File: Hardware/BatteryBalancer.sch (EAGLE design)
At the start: 49 parts, among them J2 ICSP, U3 SINGLECELL, U4 ATMEGA328P_TQFP, U5 SINGLECELL, U6 SINGLECELL, U7 SINGLECELL, Y1 16MHz

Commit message: Going home
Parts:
- removed JP10: JP10, SparkFun-Connectors:M08SMD-COMBO
- removed JP11: IOL, SparkFun-Connectors:M08SMD-COMBO
- removed JP13: AD, SparkFun-Connectors:M06SMD-STRAIGHT-COMBO
- added C11, C12, C13, C14, C18: 0.1uF, SparkFun-Capacitors:0.1UF-0603-25V-(+80/-20%)
- added C15: 10uF, SparkFun-Capacitors:10UF-POLAR-EIA3216-16V-10%(TANT)
- added C17: 10nF, SparkFun-Capacitors:10NF-0603-50V-10%
- added D2: GREEN, SparkFun-LED:LED-GREENLILYPAD
- added D3: YELLOW, SparkFun-LED:LED-YELLOW_HIDDENSILK
- added F1: 6V 0.5A, SparkFun-Fuses:PPTC_6V500MA
- added J1: (no value), SparkFun-Connectors:USB_MICRO-B_HALF_PTH_MILL
- added LED1: Blue, SparkFun-LED:LED-BLUE_HIDDENSILK
- added R1, R24: 10k, SparkFun-Resistors:10KOHM-0603-1/10W-1%
- added R25, R26: 4.7k, SparkFun-Resistors:4.7KOHM-0603-1/10W-1%
- added U1: CH340C, SparkFun-IC-Comms:CH340C
- added U10, U11, U2, U8, U9: TAP_POINT, BBLib:TAP_POINT
- J2: value ICSP -> ISP
- R3: value 10k -> 4.7k; device SparkFun-Resistors:10KOHM-0603-1/10W-1% -> SparkFun-Resistors:4.7KOHM-0603-1/10W-1%
- S1: value RESET -> Tall Switch; device SparkFun-Electromechanical:SWITCH_SPST_4_PINSQUARE -> SparkFun-Switches:MOMENTARY-SWITCH-SPST-SMD-5.2-TALL-REDUNDANT
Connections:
- removed net 3.3V: JP10.5
- removed net 5V: C2.2, J2.2, JP10.4, JP10.7, R3.2, U4.AVCC, U4.VCC@4, U4.VCC@6
- removed net AD0: JP13.1, U4.PC0(ADC0)
- removed net AD1: JP13.2, U4.PC1(ADC1)
- removed net AD2: JP13.3, U4.PC2(ADC2)
- removed net AD3: JP13.4, U4.PC3(ADC3)
- removed net AD4/SDA: JP13.5, U4.PC4(ADC4/SDA)
- removed net AD5/SCL: JP13.6, U4.PC5(ADC5/SCL)
- removed net IO2: JP11.3, U4.PD2(INT0)
- removed net IO3: JP11.4, U4.PD3(INT1)
- removed net IO4: JP11.5, U4.PD4(XCK/T0)
- removed net IO5: JP11.6, U4.PD5(T1)
- removed net IO6: JP11.7, U4.PD6(AIN0)
- removed net IO7: JP11.8, U4.PD7(AIN1)
- removed net IO8: U4.PB0(ICP)
- removed net IO9: U4.PB1(OC1A)
- removed net VIN: JP10.1
- new net !DTR: C12.1, U1.!DTR
- new net !PD: R1.1, U$2.!PD
- new net AREF: C2.1, U4.AREF
- new net D+: J1.D+, U1.UD+
- new net D-: J1.D-, U1.UD-
- new net N$1: LED1.A, R3.2
- new net N$36: D3.A, R25.1
- new net SHLD: J1.SHIELD
- new net USBVCC: C14.1, C15.+, F1.2
- new net VBATT: R16.2, R2.2, R7.1, U$2.VDD, U11.1, U5.+
- new net VCC: C11.2, C18.1, J2.2, R24.2, R25.2, R26.2, U1.VCC, U4.AVCC, U4.VCC
- new net VUSB: C13.1, F1.1, J1.VBUS
- net GND: now also C11.1, C13.2, C14.2, C15.-, C17.2, C18.2, C2.2, J1.GND, LED1.C, U1.GND, U2.1, U4.GND; no longer C2.1, JP10.2, JP10.3, S1.2, U4.GND@3, U4.GND@5
- net N$10: now also U8.1
- net N$2: now also D2.A, R26.1; no longer R16.2, R2.2, R7.1, U$2.VDD, U5.+
- net N$23: now also R1.2
- net N$38: now also C17.1, U1.V3; no longer U$2.!PD
- net N$6: now also U10.1
- net N$8: now also U9.1
- net RESET: now also C12.2, R24.1, S1.2; no longer JP10.6, R3.1, S1.3, S1.4
- net RX-I: now also D3.C, U1.TXO; no longer JP11.1
- net SCLK: now also R3.1
- net TX-O: now also D2.C, U1.RXI; no longer JP11.2
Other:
- note added: "USB-to-Serial Converter"
- moved on the sheet: C2, J2, R3, Y1

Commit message: going home
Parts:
- added C16: 10uF, SparkFun-Capacitors:10UF-POLAR-EIA3216-16V-10%(TANT)
- added C19: 0.1uF, SparkFun-Capacitors:0.1UF-0603-25V-(+80/-20%)
- added C20: 47uF, SparkFun-Capacitors:47UF-POLAR-PANASONIC_D-35V-20%
- added D1: TH, SparkFun-DiscreteSemi:DIODE-ZENER-MMBZ5233BLT1G
- added D4: MATCH, SparkFun-DiscreteSemi:DIODE-ZENER-MMBZ5233BLT1G
- added IC1: OP-AMP, SparkFun-IC-Amplifiers:OPAMP-DUALU
- added IC3: LM1117, Testing:V_REG_LM1117ALT1
- added Q4: (no value), MTAES_V2_UniqueParts:AMP_MOSFET_NCH-2N7002K
- added Q5: 4.3A/20V/54mΩ, SparkFun-DiscreteSemi:MOSFET_PCH-IRLML2244
- added R27: 1M, SparkFun-Resistors:1MOHM-0603-1/4W-5%
- added R28: 330k, SparkFun-Resistors:330KOHM-0603-1/10W-1%
- added R29: 715, SparkFun-Resistors:715OHM-0603-1/10W-1%
- added R30: 240, SparkFun-Resistors:240OHM-0603-1/10W-1%
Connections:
- removed net VBATT: R16.2, R2.2, R7.1, U$2.VDD, U11.1, U5.+
- new net 5V: C16.+, C19.1, IC3.OUT, IC3.OUT@1, R30.2
- new net CHARGE: IC1G1.OUT
- new net N$39: IC3.ADJ, R29.2, R30.1
- new net N$40: D4.C, IC1G1.+IN, R27.1
- new net N$41: D1.C, IC1G1.-IN, R28.1
- new net V_BATT: C20.+, IC1G3.P$V+, IC3.IN, Q5.S, R27.2, R28.2
- new net V_RAW: Q5.D, R16.2, R2.2, R7.1, U$2.VDD, U11.1, U5.+
- net GND: now also C16.-, C19.2, C20.-, D1.A, D4.A, IC1G3.P$V-, Q5.G, R29.1
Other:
- note added: "P-channel MOSFET for reverse polarity protection"
- note added: "Power Supply"
- note added: "This comparator will be HIGH when the voltage is greater than the Zener voltage of the THreshold diode, and LOW otherwise. The MATCH diode is used primarily to match the leakage current of the THreshold diode. Below V THreshold the leakage currents cause substantial voltage drop over the large-value current limiting resistors, sized so that the inverting input sees a higher voltage. When the batt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"
- moved on the sheet: R17, R18, R19, R20, R21, R22, R23

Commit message: Schematic mostly done, starting layout
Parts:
- removed IC3: LM1117, Testing:V_REG_LM1117ALT1
- removed Q4: (no value), MTAES_V2_UniqueParts:AMP_MOSFET_NCH-2N7002K
- removed R20, R21, R22: 10k, SparkFun-Resistors:10KOHM-0603-1/10W-1%
- added C21: 1.0uF, SparkFun-Capacitors:1.0UF-1206-50V-10%
- added D10, D11, D7, D8, D9: BLUE, SparkFun-LED:LED-BLUE0603
- added D5, D6: 3A/10V/280mV, SparkFun-DiscreteSemi:DIODE-SCHOTTKY-BAT60A
- added JP1: VCC, SparkFun-Jumpers:JUMPER-SMT_2_NC_TRACE_SILK
- added Q6: (no value), MTAES_V2_UniqueParts:AMP_MOSFET_NCH-2N7002K
- added R31, R32: 1k, SparkFun-Resistors:1KOHM-0603-1/10W-1%
- added R33, R34, R35: 10k, SparkFun-Resistors:10KOHM-0603-1/10W-1%
- added R40, R41, R42, R43: DNP, SparkFun-Resistors:1KOHM-HORIZ-1/4W-5%
- added S2: Force Charge, SparkFun-Switches:MOMENTARY-SWITCH-SPST-SMD-5.2-TALL-REDUNDANT
- added S3: TEST, SparkFun-Switches:MOMENTARY-SWITCH-SPST-SMD-5.2-TALL-REDUNDANT
- added U$1: MCP1755, BBLib:MCP1755
- C15, C16: value 10uF -> 1.0uF; device SparkFun-Capacitors:10UF-POLAR-EIA3216-16V-10%(TANT) -> SparkFun-Capacitors:1.0UF-0603-16V-10%-X7R
- C19: device SparkFun-Capacitors:0.1UF-0603-25V-(+80/-20%) -> SparkFun-Capacitors:0.1UF-0603-25V-5%
- C20: value 47uF -> 10uF; device SparkFun-Capacitors:47UF-POLAR-PANASONIC_D-35V-20% -> SparkFun-Capacitors:10UF-1210-50V-20%
- Q5: value 4.3A/20V/54mΩ -> MOSFET_PCH-IRLML2244
- R1, R24: value 10k -> 1k; device SparkFun-Resistors:10KOHM-0603-1/10W-1% -> SparkFun-Resistors:1KOHM-0603-1/10W-1%
- R29: value 715 -> 10k; device SparkFun-Resistors:715OHM-0603-1/10W-1% -> SparkFun-Resistors:10KOHM-0603-1/10W-1%
- R30: value 240 -> 10k; device SparkFun-Resistors:240OHM-0603-1/10W-1% -> SparkFun-Resistors:10KOHM-0603-1/10W-1%
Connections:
- removed net !PD: R1.1, U$2.!PD
- removed net N$35: R22.2, U$2.AUX1
- removed net SCK: J2.3
- new net !CVNST: R34.1, U$2.!CNVST, U4.ADC7
- new net LED1: D7.A, U4.PC0(ADC0)
- new net LED2: D8.A, U4.PC1(ADC1)
- new net LED3: D9.A, U4.PC2(ADC2)
- new net LED4: D10.A, U4.PC3(ADC3)
- new net N$42: D9.C, R31.2
- new net N$43: D8.C, R24.2
- new net N$44: D7.C, R1.2
- new net TEST: D11.A, S3.1, U4.ADC6
- net !CS: now also R35.1
- net 5V: now also C16.1, D5.A, JP1.1, U$1.OUT; no longer C16.+, IC3.OUT, IC3.OUT@1, R30.2
- net ALERT: now also R33.1, U4.PD2(INT0)
- net CHARGE: now also Q6.D
- net GND: now also C15.2, C16.2, C20.2, C21.2, R1.1, R19.1, R23.1, R24.1, R31.1, R32.1, U$1.GND; no longer C15.-, C16.-, C20.-, R29.1
- net N$23: now also R43.2, U$2.AUX1; no longer C6.1, C7.1, C8.1, R1.2, U$2.AVCC, U$2.DVCC, U$2.VDRIVE, U$2.VREG
- net N$32: now also R42.2, U$2.AUX2; no longer R19.2, U$2.AUX4
- net N$33: now also R41.2; no longer R20.2
- net N$34: now also R40.2, U$2.AUX4; no longer R21.2, U$2.AUX2
- net N$37: now also D11.C, R19.2; no longer U$2.!CNVST
- net N$39: now also D10.C, R32.2; no longer IC3.ADJ, R29.2, R30.1
- net N$40: now also S2.1
- net RESET: now also Q6.S, R29.1, U$1.!SHDWN, U$2.!PD; no longer R24.1
- net SCLK: now also J2.3
- net USBVCC: now also C15.1, D6.A; no longer C15.+
- net VCC: now also D5.C, D6.C, JP1.2, Q6.G, R29.2, R33.2, R34.2, R35.2, S3.2; no longer R24.2
- net VREG: now also C6.1, C7.1, C8.1, R40.1, R41.1, R42.1, R43.1, U$2.AVCC, U$2.DVCC, U$2.VDRIVE, U$2.VREG; no longer R19.1, R20.1, R21.1, R22.1, R23.1
- net V_BATT: now also R30.2, S2.2, U$1.IN; no longer C20.+, IC3.IN
- net V_RAW: now also C20.1, C21.1
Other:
- note added: "Cut jumper is using USB-Serial"
- note added: "Maybe in the future this could incorporate a Schmitt Trigger to prevent switching too often"
- note added: "Probably don't need a pull on the op-amp line"
- note added: "This level shifter controls the reset line with the charge signal. When not charging Reset goes low. Reset has a pullup to VCC"
- note removed: "Power Supply"
- moved on the sheet: C1, C10, C19, C3, C4, C5, C6, C7, C8, C9, IC1G1, IC1G2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

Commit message: Routed 90%
Needs finishing routing and also pretty graphics
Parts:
- removed C15: 1.0uF, SparkFun-Capacitors:1.0UF-0603-16V-10%-X7R
- removed D10, D11: BLUE, SparkFun-LED:LED-BLUE0603
- removed F1: 6V 0.5A, SparkFun-Fuses:PPTC_6V500MA
- removed LED1: Blue, SparkFun-LED:LED-BLUE_HIDDENSILK
- removed Q10: (no value), MTAES_V2_UniqueParts:AMP_MOSFET_NCH-2N7002K
- removed R34, R35: 10k, SparkFun-Resistors:10KOHM-0603-1/10W-1%
- removed R40, R41, R42, R43: DNP, SparkFun-Resistors:1KOHM-HORIZ-1/4W-5%
- removed U$1: MCP1755, BBLib:MCP1755
- removed U$2: AD7280A, BBLib:AD7280A
- added JP2: RPP_BYP, SparkFun-Jumpers:JUMPER-SMT_2_NC_TRACE_SILK
- added Q4: (no value), MTAES_V2_UniqueParts:AMP_MOSFET_NCH-2N7002K
- added R20, R21, R22: DNP, BBLib:NTC_STOP_ONE_SIDE
- added U12: ATMEGA328P_TQFP, SparkFun-IC-Microcontroller:ATMEGA328P_TQFP
- added U13: CH340C, SparkFun-IC-Comms:CH340C
- C1: value 0.1uF -> 10uF; device SparkFun-Capacitors:0.1UF-0603-25V-5% -> SparkFun-Capacitors:10UF-1210-50V-20%
- C10, C6: value 1.0uF -> 0.1uF; device SparkFun-Capacitors:1.0UF-0603-16V-10%-X7R -> SparkFun-Capacitors:0.1UF-0603-25V-5%
- C11, C13: value 0.1uF -> 1.0uF; device SparkFun-Capacitors:0.1UF-0603-25V-(+80/-20%) -> SparkFun-Capacitors:1.0UF-0603-16V-10%-X7R
- C12: device SparkFun-Capacitors:0.1UF-0603-25V-(+80/-20%) -> SparkFun-Capacitors:0.1UF-0603-25V-5%
- C16: value 1.0uF -> 0.1uF; device SparkFun-Capacitors:1.0UF-0603-16V-10%-X7R -> SparkFun-Capacitors:0.1UF-0603-25V-(+80/-20%)
- C17: value 10nF -> 0.1uF; device SparkFun-Capacitors:10NF-0603-50V-10% -> SparkFun-Capacitors:0.1UF-0603-25V-(+80/-20%)
- C19, C7: value 0.1uF -> 1.0uF; device SparkFun-Capacitors:0.1UF-0603-25V-5% -> SparkFun-Capacitors:1.0UF-0603-16V-10%-X7R
- C2: value 0.1uF -> 1.0uF; device SparkFun-Capacitors:0.1UF-0603-25V-(+80/-20%) -> SparkFun-Capacitors:1.0UF-1206-50V-10%
- C20: value 10uF -> 0.1uF; device SparkFun-Capacitors:10UF-1210-50V-20% -> SparkFun-Capacitors:0.1UF-0603-25V-(+80/-20%)
- C21: value 1.0uF -> 10nF; device SparkFun-Capacitors:1.0UF-1206-50V-10% -> SparkFun-Capacitors:10NF-0603-50V-10%
- D1: value TH -> MATCH
- D2: value GREEN -> TH; device SparkFun-LED:LED-GREENLILYPAD -> SparkFun-DiscreteSemi:DIODE-ZENER-MMBZ5233BLT1G
- D3: value YELLOW -> 3A/10V/280mV; device SparkFun-LED:LED-YELLOW_HIDDENSILK -> SparkFun-DiscreteSemi:DIODE-SCHOTTKY-BAT60A
- D4: value MATCH -> BLUE; device SparkFun-DiscreteSemi:DIODE-ZENER-MMBZ5233BLT1G -> SparkFun-LED:LED-BLUE0603
- D5, D6: value 3A/10V/280mV -> BLUE; device SparkFun-DiscreteSemi:DIODE-SCHOTTKY-BAT60A -> SparkFun-LED:LED-BLUE0603
- D9: value BLUE -> 3A/10V/280mV; device SparkFun-LED:LED-BLUE0603 -> SparkFun-DiscreteSemi:DIODE-SCHOTTKY-BAT60A
- Q1: value (none) -> MOSFET_PCH-IRLML2244; device MTAES_V2_UniqueParts:AMP_MOSFET_NCH-2N7002K -> SparkFun-DiscreteSemi:MOSFET_PCH-IRLML2244
- Q5: value MOSFET_PCH-IRLML2244 -> (none); device SparkFun-DiscreteSemi:MOSFET_PCH-IRLML2244 -> MTAES_V2_UniqueParts:AMP_MOSFET_NCH-2N7002K
- R1: value 1k -> 10; device SparkFun-Resistors:1KOHM-0603-1/10W-1% -> SparkFun-Resistors:10OHM-1206-1/4W-1%
- R10: value 10k -> 1M; device SparkFun-Resistors:10KOHM-0603-1/10W-1% -> SparkFun-Resistors:1MOHM-0603-1/4W-5%
- R15: value 10k -> 330k; device SparkFun-Resistors:10KOHM-0603-1/10W-1% -> SparkFun-Resistors:330KOHM-0603-1/10W-1%
- R19: value 10k -> DNP; device SparkFun-Resistors:10KOHM-0603-1/10W-1% -> BBLib:NTC_STOP_ONE_SIDE
- R24: value 1k -> 10k; device SparkFun-Resistors:1KOHM-0603-1/10W-1% -> SparkFun-Resistors:10KOHM-0603-1/10W-1%
- R25, R26: value 4.7k -> 10k; device SparkFun-Resistors:4.7KOHM-0603-1/10W-1% -> SparkFun-Resistors:10KOHM-0603-1/10W-1%
- R27: value 1M -> 10k; device SparkFun-Resistors:1MOHM-0603-1/4W-5% -> SparkFun-Resistors:10KOHM-0603-1/10W-1%
- R28: value 330k -> 10k; device SparkFun-Resistors:330KOHM-0603-1/10W-1% -> SparkFun-Resistors:10KOHM-0603-1/10W-1%
- R3: value 4.7k -> 10; device SparkFun-Resistors:4.7KOHM-0603-1/10W-1% -> SparkFun-Resistors:10OHM-1206-1/4W-1%
- R30, R33: value 10k -> 1k; device SparkFun-Resistors:10KOHM-0603-1/10W-1% -> SparkFun-Resistors:1KOHM-0603-1/10W-1%
- R5, R6: value 10 -> 10k; device SparkFun-Resistors:10OHM-1206-1/4W-1% -> SparkFun-Resistors:10KOHM-0603-1/10W-1%
- S1: value Tall Switch -> Force Charge
- S2: value Force Charge -> TEST
- S3: value TEST -> Tall Switch
- U1: value CH340C -> TAP_POINT; device SparkFun-IC-Comms:CH340C -> BBLib:TAP_POINT
- U10: value TAP_POINT -> MCP1755; device BBLib:TAP_POINT -> BBLib:MCP1755
- U11: value TAP_POINT -> AD7280A; device BBLib:TAP_POINT -> BBLib:AD7280A
- U3, U5: value SINGLECELL -> TAP_POINT; device BBLib:SINGLECELL -> BBLib:TAP_POINT
- U4: value ATMEGA328P_TQFP -> TAP_POINT; device SparkFun-IC-Microcontroller:ATMEGA328P_TQFP -> BBLib:TAP_POINT
- U8, U9: value TAP_POINT -> SINGLECELL; device BBLib:TAP_POINT -> BBLib:SINGLECELL
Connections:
- removed net N$1: LED1.A, R3.2
- removed net N$2: D2.A, R26.1
- removed net N$36: D3.A, R25.1
- removed net VUSB: C13.1, F1.1, J1.VBUS
- net !CS: now also R28.1, U11.!CS, U12.PB2(SS/OC1B); no longer R35.1, U$2.!CS, U4.PB2(SS/OC1B)
- net !CVNST: now also R27.1, U11.!CNVST, U12.ADC7; no longer R34.1, U$2.!CNVST, U4.ADC7
- net !DTR: now also C14.1, U13.!DTR; no longer C12.1, U1.!DTR
- net 5V: now also C7.1, C8.1, D3.A, U10.OUT; no longer C16.1, C19.1, D5.A, U$1.OUT
- net ALERT: now also R29.1, U11.ALERT, U12.PD2(INT0); no longer R33.1, U$2.ALERT, U4.PD2(INT0)
- net AREF: now also C16.1, U12.AREF; no longer C2.1, U4.AREF
- net CHARGE: now also R24.1
- net D+: now also U13.UD+; no longer U1.UD+
- net D-: now also U13.UD-; no longer U1.UD-
- net GND: now also C1.2, C11.2, C12.2, C17.1, D2.A, Q1.G, Q5.S, R26.1, R30.1, R33.1, R9.1, S3.1, U10.GND, U11.AGND, U11.ALERT_LO, U11.DGND, U11.REFGND, U11.VSS, U12.AGND, U12.GND, U13.GND, U5.1, U9.-; no longer C11.1, C14.2, C15.2, C17.2, C6.2, D4.A, LED1.C, Q3.S, Q5.G, R1.1, R15.1, R19.1, R24.1, S1.1, U$1.GND, U$2.AGND, U$2.ALERT_LO, U$2.DGND, U$2.REFGND, U$2.VSS, U1.GND, U2.1, U4.AGND, U4.GND, U7.-
- net LED1: now also D5.A, U12.PC0(ADC0); no longer D7.A, U4.PC0(ADC0)
- net LED2: now also D6.A, U12.PC1(ADC1); no longer D8.A, U4.PC1(ADC1)
- net LED3: now also D7.A, U12.PC2(ADC2); no longer D9.A, U4.PC2(ADC2)
- net LED4: now also D8.A, U12.PC3(ADC3); no longer D10.A, U4.PC3(ADC3)
- net MISO: now also U11.SDO, U12.PB4(MISO); no longer U$2.SDO, U4.PB4(MISO)
- net MOSI: now also U11.SDI, U12.PB3(MOSI/OC2); no longer U$2.SDI, U4.PB3(MOSI/OC2)
- net N$10: now also Q4.S, R4.2, R8.1, U4.1, U8.-, U9.+; no longer Q2.S, R10.1, R6.2, U6.-, U7.+, U8.1
- net N$11: now also Q5.D, R4.1; no longer Q3.D, R6.1
- net N$12: now also Q2.G; no longer Q10.G
- net N$13: now also Q3.G; no longer Q1.G
- net N$14: now also U11.MASTER; no longer U$2.MASTER
- net N$15: now also Q4.G; no longer Q2.G
- net N$16: now also Q5.G; no longer Q3.G
- net N$17: now also C6.2, R9.2, U11.VIN0; no longer C1.2, R15.2, U$2.VIN0
- net N$18: now also U11.CB1; no longer U$2.CB1
- net N$19: now also C5.2, C6.1, R8.2, U11.VIN1; no longer C1.1, C3.2, R10.2, U$2.VIN1
- net N$20: now also U11.CB2; no longer U$2.CB2
- net N$21: now also C5.1, R7.2, U11.VIN2; no longer C3.1, R9.2, U$2.VIN2
- net N$22: now also U11.CB3; no longer U$2.CB3
- net N$23: now also R22.2, U11.AUX1; no longer R43.2, U$2.AUX1
- net N$24: now also U11.CB4; no longer U$2.CB4
- net N$25: now also C3.1, R5.2, U11.VIN6; no longer C5.1, R7.2, U$2.VIN6
- net N$26: now also C3.2, R6.2, U11.VIN3, U11.VIN4, U11.VIN5; no longer C5.2, R8.2, U$2.VIN3, U$2.VIN4, U$2.VIN5
- net N$27: now also U11.VREF; no longer U$2.VREF
- net N$28: now also U11.AUX6; no longer U$2.AUX6
- net N$29: now also C11.1, U11.CREF; no longer C10.1, U$2.CREF
- net N$3: now also U12.PB6(XTAL1/TOSC1); no longer U4.PB6(XTAL1/TOSC1)
- net N$30: now also U11.AUX_TERM; no longer U$2.AUX_TERM
- net N$31: now also U11.AUX5; no longer U$2.AUX5
- net N$32: now also R21.2, U11.AUX2; no longer R42.2, U$2.AUX2
- net N$33: now also R20.2, U11.AUX3; no longer R41.2, U$2.AUX3
- net N$34: now also R19.2, U11.AUX4; no longer R40.2, U$2.AUX4
- net N$37: now also D4.C, R26.2; no longer D11.C, R19.2
- net N$38: now also C21.1, U13.V3; no longer C17.1, U1.V3
- net N$39: now also D8.C, R33.2; no longer D10.C, R32.2
- net N$4: now also U12.PB7(XTAL2/TOSC2); no longer U4.PB7(XTAL2/TOSC2)
- net N$40: now also D1.C, R10.1, S1.1; no longer D4.C, R27.1, S2.1
- net N$41: now also D2.C, R15.1; no longer D1.C, R28.1
- net N$42: now also D7.C, R32.2; no longer D9.C, R31.2
- net N$43: now also D6.C, R31.2; no longer D8.C, R24.2
- net N$44: now also D5.C, R30.2; no longer D7.C, R1.2
- net N$5: now also Q2.D, R1.1; no longer Q10.D, R2.1
- net N$6: now also Q2.S, R2.2, R6.1, U2.1, U6.-, U7.+; no longer Q10.S, R4.2, R8.1, U10.1, U3.+, U5.-
- net N$7: now also Q3.D, R2.1; no longer Q1.D, R4.1
- net N$8: now also Q3.S, R3.2, R7.1, U3.1, U7.-, U8.+; no longer Q1.S, R5.2, R9.1, U3.-, U6.+, U9.1
- net N$9: now also Q4.D, R3.1; no longer Q2.D, R5.1
- net RESET: now also C14.2, R25.1, S3.2, U10.!SHDWN, U11.!PD, U12.PC6(/RESET); no longer C12.2, R29.1, S1.2, U$1.!SHDWN, U$2.!PD, U4.PC6(/RESET)
- net RX-I: now also U12.PD0(RXD), U13.TXO; no longer D3.C, U1.TXO, U4.PD0(RXD)
- net SCLK: now also U11.SCLK, U12.PB5(SCK); no longer R3.1, U$2.SCLK, U4.PB5(SCK)
- net TEST: now also D4.A, S2.1, U12.PD3(INT1); no longer D11.A, S3.1, U4.ADC6
- net TX-O: now also U12.PD1(TXD), U13.RXI; no longer D2.C, U1.RXI, U4.PD1(TXD)
- net USBVCC: now also C18.1, C19.1, D9.A, J1.VBUS; no longer C14.1, C15.1, D6.A, F1.2
- net VCC: now also C17.2, C20.1, D3.C, D9.C, R27.2, R28.2, S2.2, U12.AVCC, U12.VCC, U13.VCC; no longer C11.2, C18.1, D5.C, D6.C, R26.2, R33.2, R34.2, R35.2, S3.2, U1.VCC, U4.AVCC, U4.VCC
- net VREG: now also C10.1, C12.1, C13.1, R19.1, R20.1, R21.1, R22.1, U11.AVCC, U11.DVCC, U11.VDRIVE, U11.VREG; no longer C6.1, C7.1, C8.1, R40.1, R41.1, R42.1, R43.1, U$2.AVCC, U$2.DVCC, U$2.VDRIVE, U$2.VREG
- net V_BATT: now also JP2.2, Q1.S, R10.2, R15.2, R24.2, S1.2, U10.IN; no longer Q5.S, R27.2, R28.2, R30.2, S2.2, U$1.IN
- net V_RAW: now also C1.1, C2.1, JP2.1, Q1.D, R1.2, R5.1, U1.1, U11.VDD, U6.+; no longer C20.1, C21.1, Q5.D, R2.2, R7.1, U$2.VDD, U11.1, U5.+
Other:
- moved on the sheet: C1, C10, C11, C12, C13, C14, C16, C17, C18, C19, C2, C20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

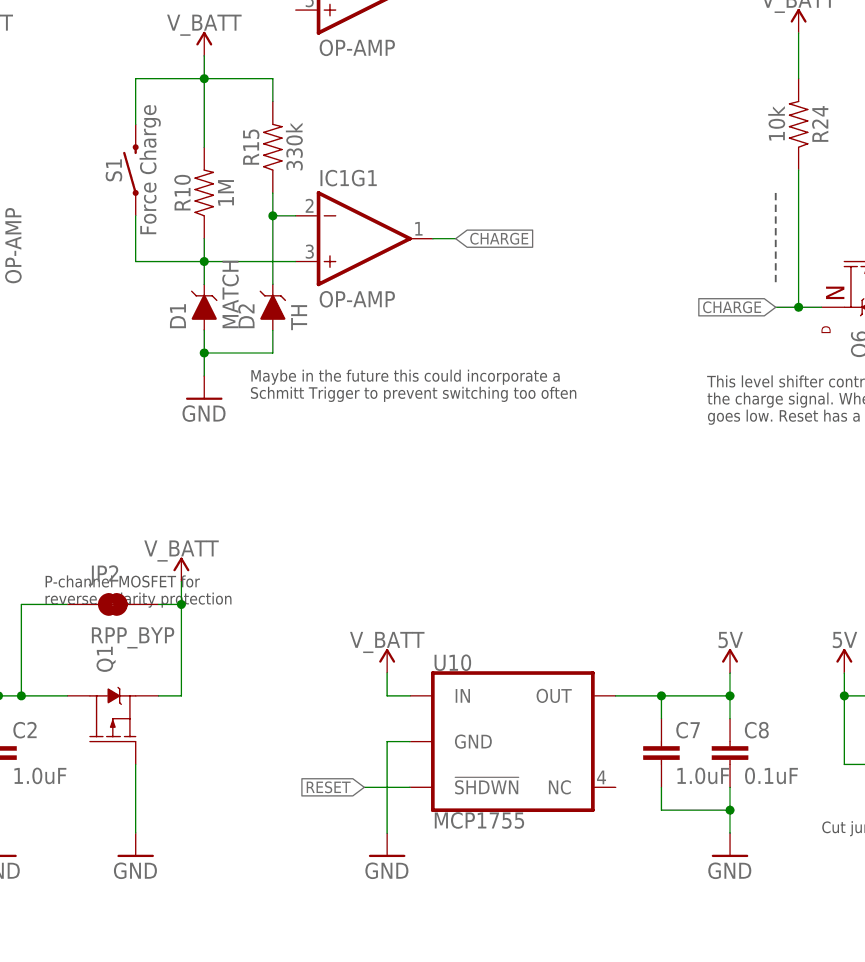
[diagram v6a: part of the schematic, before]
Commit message: Implement LV shutoff circuit changes in schematic
Switch to voltage-divider/zener comparator, change regulator enable to raw compararator output
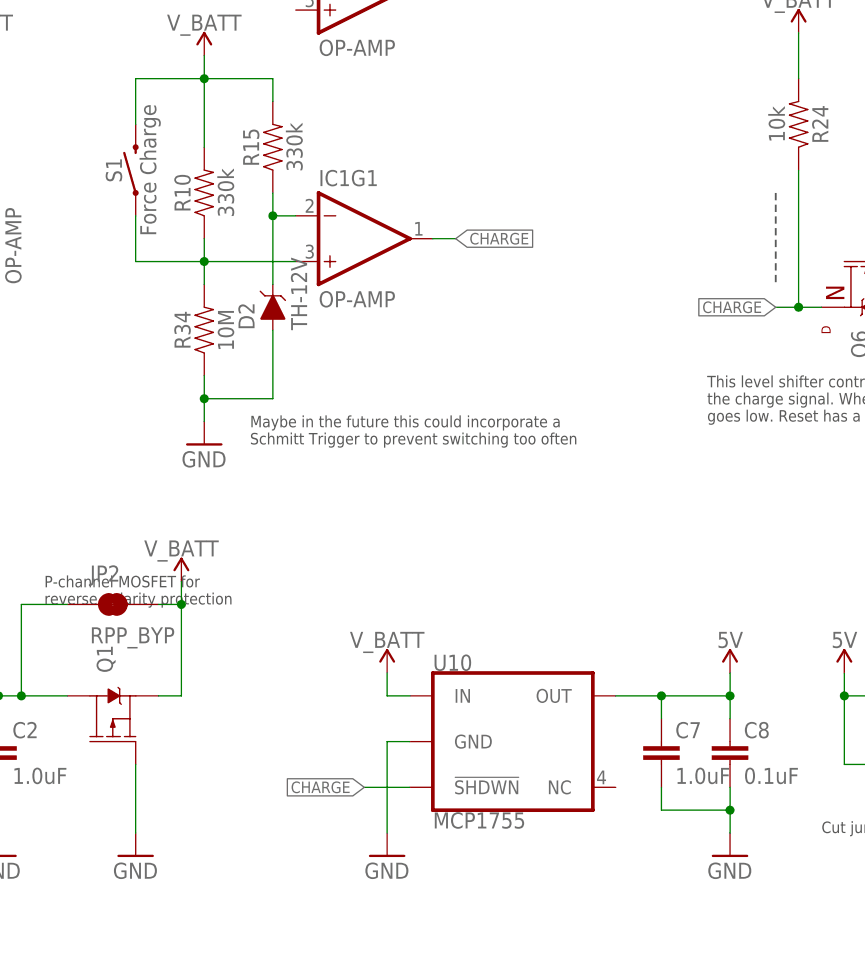
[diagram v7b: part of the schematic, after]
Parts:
- removed D1: MATCH, SparkFun-DiscreteSemi:DIODE-ZENER-MMBZ5233BLT1G
- added R34: 10M, SparkFun-Resistors:10MOHM-0603-1/10W-5%
- D2: value TH -> TH-12V
- R10: value 1M -> 330k; device SparkFun-Resistors:1MOHM-0603-1/4W-5% -> SparkFun-Resistors:330KOHM-0603-1/10W-1%
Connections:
- net CHARGE: now also U10.!SHDWN
- net GND: now also R34.1; no longer D1.A
- net N$40: now also R34.2; no longer D1.C
- net RESET: no longer U10.!SHDWN

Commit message: Panelized + cammed
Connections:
- net RESET renamed !RESET
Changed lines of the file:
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@@
 </segment>
 </net>
-<net name="RESET" class="0">
+<net name="!RESET" class="0">
 <segment>
 <wire x1="307.34" y1="175.26" x2="304.8" y2="175.26" width="0.1524" layer="91"/>
